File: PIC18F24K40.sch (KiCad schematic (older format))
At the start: 5 parts

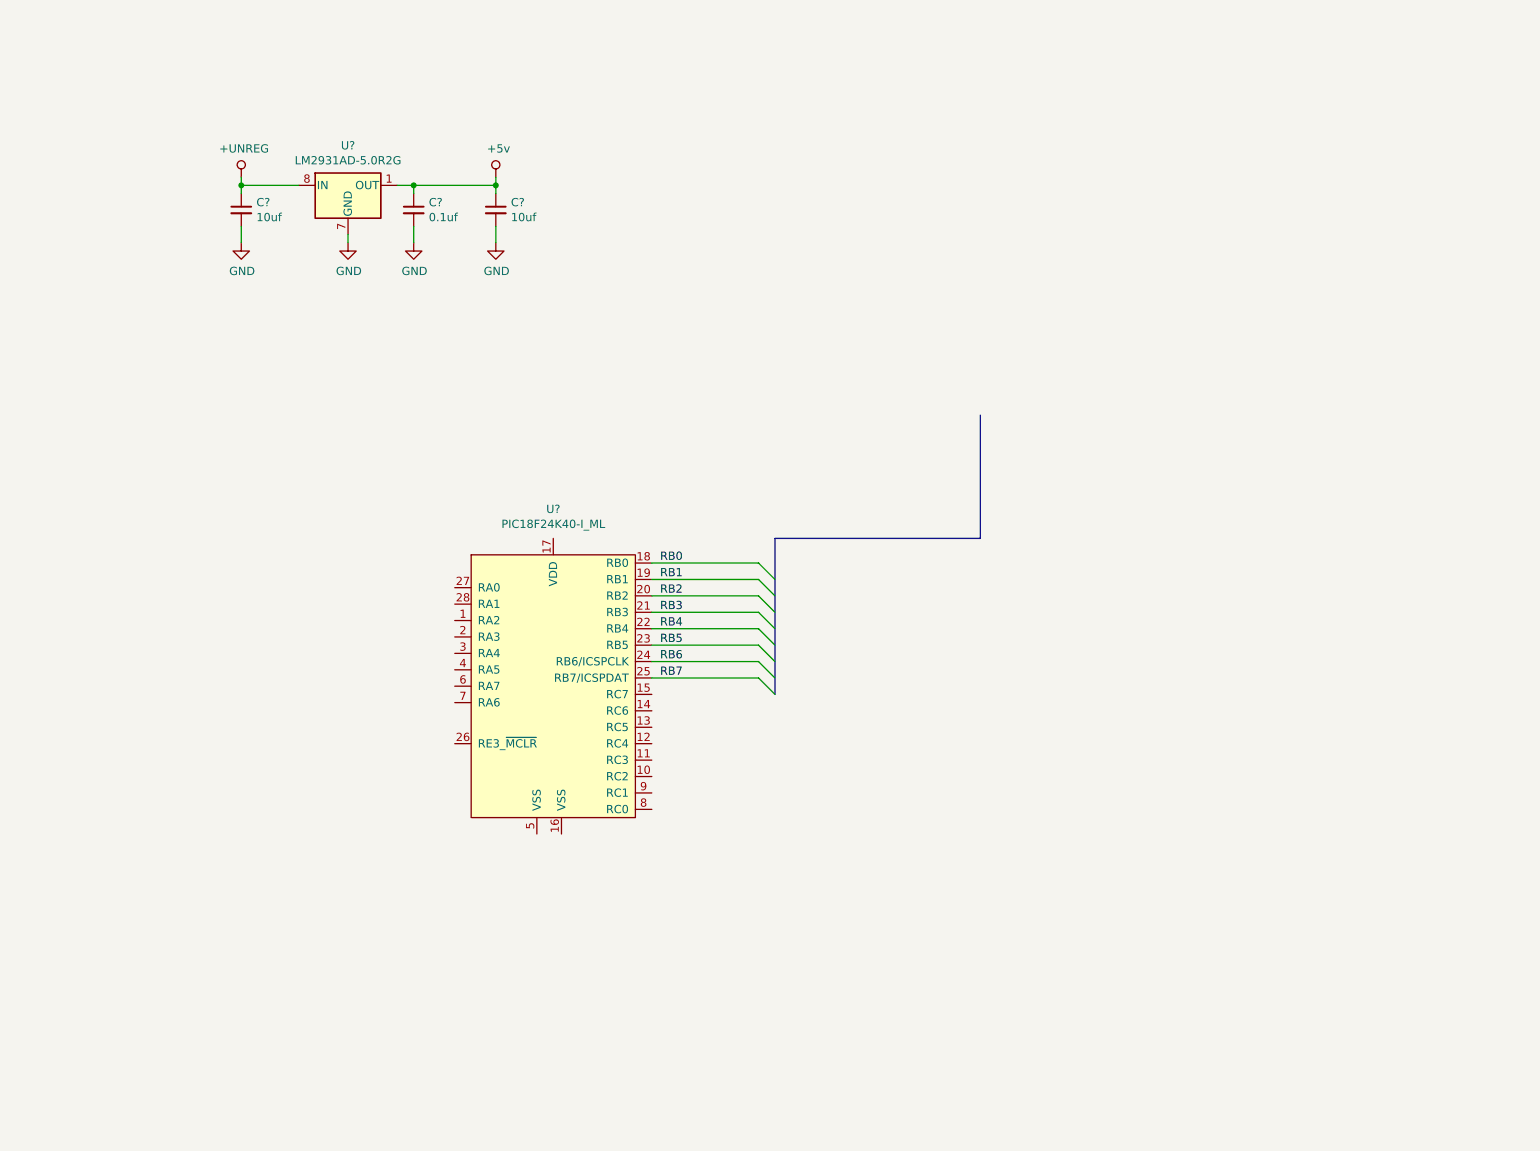
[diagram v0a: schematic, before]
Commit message: test board layout
I think I may want to drop the regulator
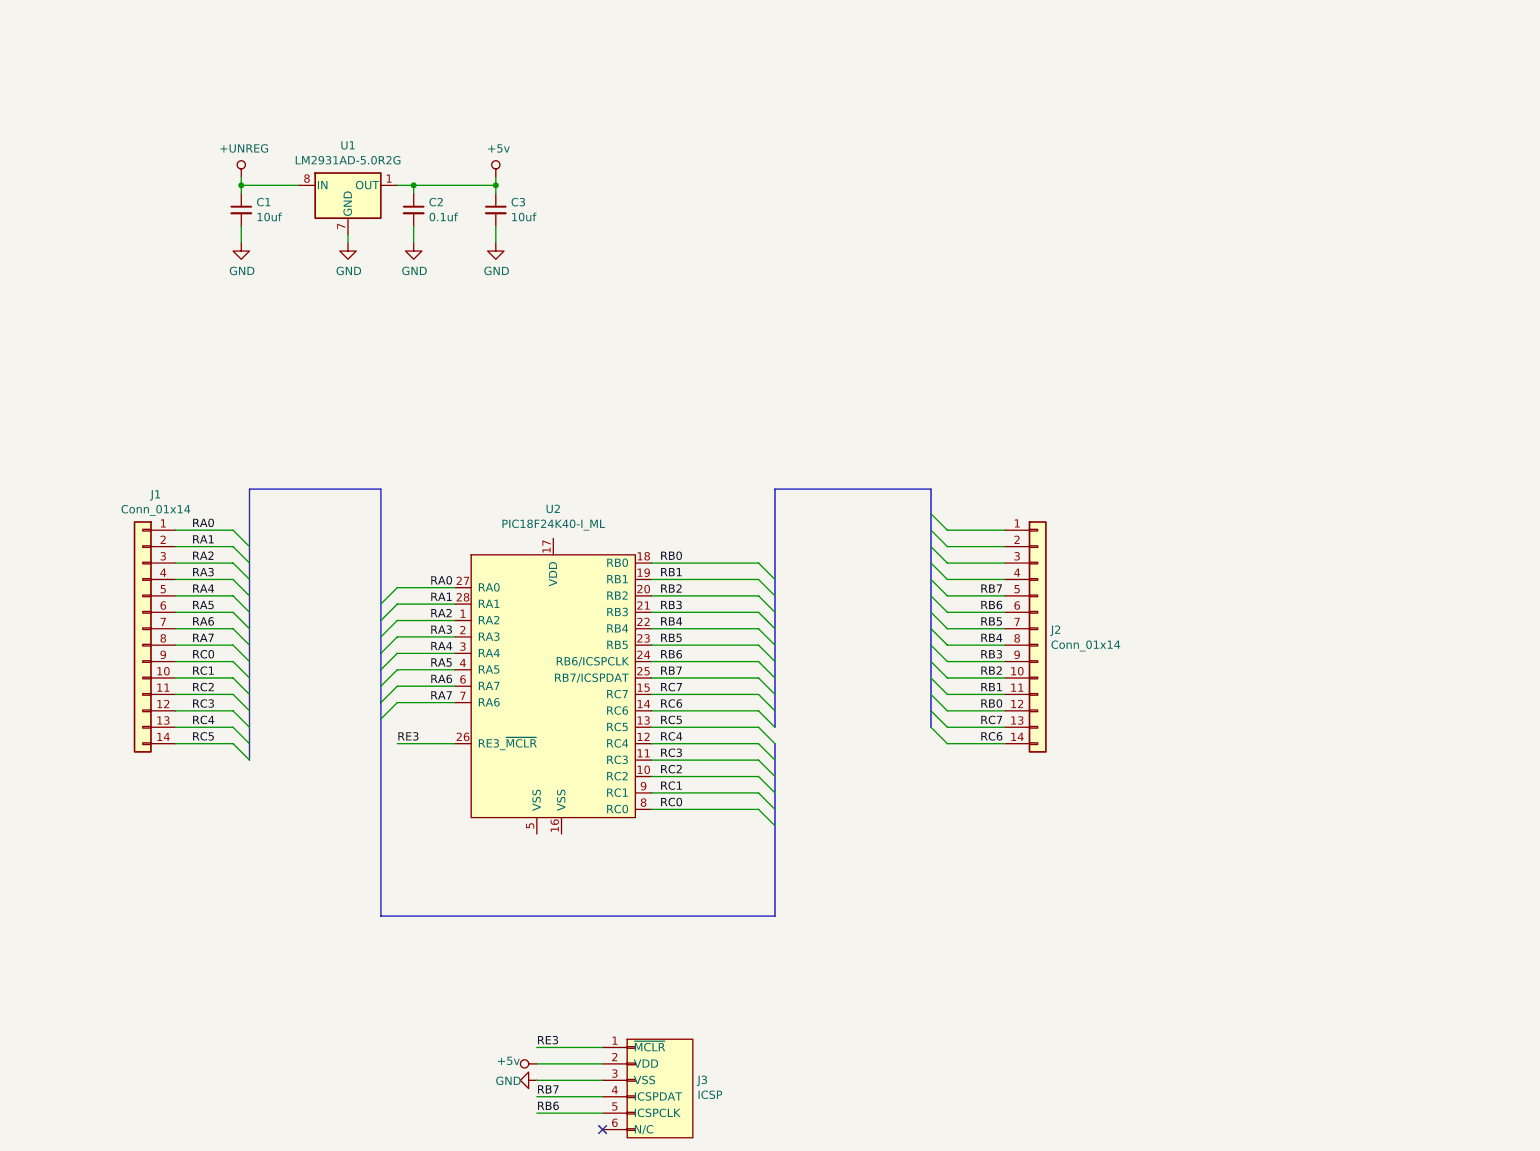
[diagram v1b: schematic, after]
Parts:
- added J1, J2: Conn_01x14, _PIC18F24K40:PinHeader_1x14_P2.54mm_Vertical, symbol _PIC18F24K40:Conn_01x14
- added J3: ICSP, _PIC18F24K40:PinHeader_1x06_P2.54mm_Vertical, symbol _PIC18F24K40:ICSP
- C1, C2, C3: renamed from C?; footprint (none) -> _PIC18F24K40:C_0603_1608Metric_Pad1.05x0.95mm_HandSolder
- U1: renamed from U?; footprint Package_SO:SOIC-8_3.9x4.9mm_P1.27mm -> _PIC18F24K40:SOIC-8_3.9x4.9mm_P1.27mm
- U2: renamed from U?; footprint (none) -> _PIC18F24K40:QFN-28-1EP_6x6mm_P0.65mm_EP4.25x4.25mm
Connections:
- net GND: now also J3.3 (VSS)
- net RB0: now also J2.12 (Pin_12)
- net RB1: now also J2.11 (Pin_11)
- net RB2: now also J2.10 (Pin_10)
- net RB3: now also J2.9 (Pin_9)
- net RB4: now also J2.8 (Pin_8)
- net RB5: now also J2.7 (Pin_7)
- net RB6: now also J2.6 (Pin_6), J3.5 (ICSPCLK)
- net RB7: now also J2.5 (Pin_5), J3.4 (ICSPDAT)
- net VCC: now also J3.2 (VDD)
- net RA2: now reaches U2.1 (RA2)
- net RA2: now also J1.3 (Pin_3)
- net RC2: now reaches U2.10 (RC2)
- net RC2: now also J1.11 (Pin_11)
- net RC3: now reaches U2.11 (RC3)
- net RC3: now also J1.12 (Pin_12)
- net RC4: now reaches U2.12 (RC4)
- net RC4: now also J1.13 (Pin_13)
- net RC5: now reaches U2.13 (RC5)
- net RC5: now also J1.14 (Pin_14)
- net RC6: now reaches U2.14 (RC6)
- net RC6: now also J2.14 (Pin_14)
- net RC7: now reaches U2.15 (RC7)
- net RC7: now also J2.13 (Pin_13)
- net RA3: now reaches U2.2 (RA3)
- net RA3: now also J1.4 (Pin_4)
- net RE3: now reaches U2.26 (RE3_~MCLR)
- net RE3: now also J3.1 (~MCLR)
- net RA0: now reaches U2.27 (RA0)
- net RA0: now also J1.1 (Pin_1)
- net RA1: now reaches U2.28 (RA1)
- net RA1: now also J1.2 (Pin_2)
- net RA4: now reaches U2.3 (RA4)
- net RA4: now also J1.5 (Pin_5)
- net RA5: now reaches U2.4 (RA5)
- net RA5: now also J1.6 (Pin_6)
- net RA6: now reaches U2.6 (RA7)
- net RA6: now also J1.7 (Pin_7)
- net RA7: now reaches U2.7 (RA6)
- net RA7: now also J1.8 (Pin_8)
- net RC0: now reaches U2.8 (RC0)
- net RC0: now also J1.9 (Pin_9)
- net RC1: now reaches U2.9 (RC1)
- net RC1: now also J1.10 (Pin_10)
- no-connect marks 0 -> 1

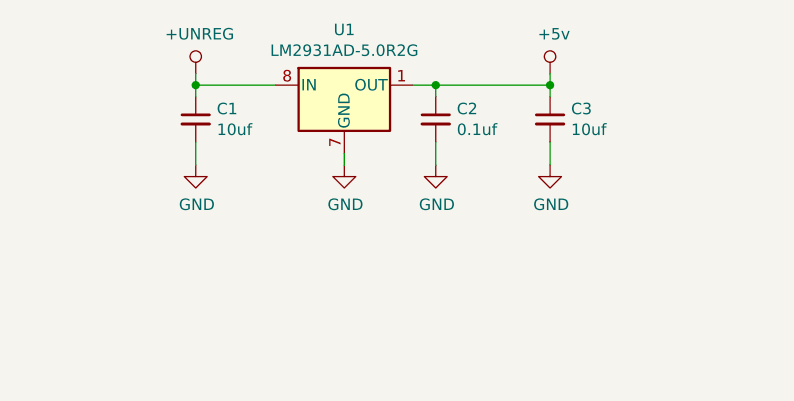
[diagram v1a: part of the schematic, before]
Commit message: Regulator removed
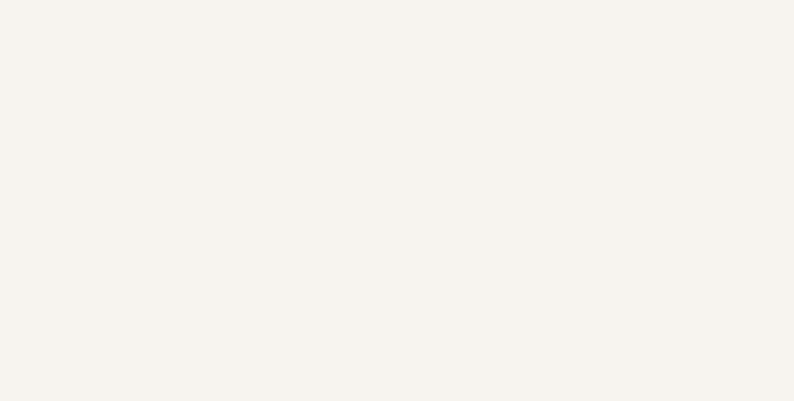
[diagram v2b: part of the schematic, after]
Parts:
- removed C1, C3: 10uf, _PIC18F24K40:C_0603_1608Metric_Pad1.05x0.95mm_HandSolder, symbol _PIC18F24K40:C_Small
- removed C2: 0.1uf, _PIC18F24K40:C_0603_1608Metric_Pad1.05x0.95mm_HandSolder, symbol _PIC18F24K40:C_Small
- removed U1: LM2931AD-5.0R2G, _PIC18F24K40:SOIC-8_3.9x4.9mm_P1.27mm, symbol _PIC18F24K40:LM2931AD-5.0R2G
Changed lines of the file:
@@
 $EndBitmap
-$Comp
-L _PIC18F24K40:LM2931AD-5.0R2G U1
-U 1 1 5BCEECB0
-P 2700 1600
-F 0 "U1" H 2700 1842 50  0000 C CNN
-F 1 "LM2931AD-5.0R2G" H 2700 1751 50  0000 C CNN
-F 2 "_PIC18F24K40:SOIC-8_3.9x4.9mm_P1.27mm" H 2800 1800 50  0001 C CIN
-F 3 "https://www.onsemi.com/pub/Collateral/LM2931-D.PDF" H 2900 1600 50  0001 C CNN
-	1    2700 1600
-	1    0    0    -1
-$EndComp
-$Comp
-L _PIC18F24K40:+UNREG #PWR0101
-U 1 1 5BCEF4FE
-P 2050 1550
-F 0 "#PWR0101" H 2050 1400 50  0001 C CNN
-F 1 "+UNREG" H 2067 1723 50  0000 C CNN
-F 2 "" H 2050 1550 50  0001 C CNN
-F 3 "" H 2050 1550 50  0001 C CNN
-	1    2050 1550
-	1    0    0    -1
-$EndComp
-$Comp
-L _PIC18F24K40:+5v #PWR0102
-U 1 1 5BCEF52A
-P 3600 1550
-F 0 "#PWR0102" H 3600 1400 50  0001 C CNN
-F 1 "+5v" H 3617 1723 50  0000 C CNN
-F 2 "" H 3600 1550 50  0001 C CNN
-F 3 "" H 3600 1550 50  0001 C CNN
-	1    3600 1550
-	1    0    0    -1
-$EndComp
-$Comp
-L _PIC18F24K40:C_Small C1
-U 1 1 5BCEF556
-P 2050 1750
-F 0 "C1" H 2142 1796 50  0000 L CNN
-F 1 "10uf" H 2142 1705 50  0000 L CNN
-F 2 "_PIC18F24K40:C_0603_1608Metric_Pad1.05x0.95mm_HandSolder" H 2050 1750 50  0001 C CNN
-F 3 "~" H 2050 1750 50  0001 C CNN
-	1    2050 1750
-	1    0    0    -1
-$EndComp
-$Comp
-L _PIC18F24K40:C_Small C2
-U 1 1 5BCEF5B4
-P 3100 1750
-F 0 "C2" H 3192 1796 50  0000 L CNN
-F 1 "0.1uf" H 3192 1705 50  0000 L CNN
-F 2 "_PIC18F24K40:C_0603_1608Metric_Pad1.05x0.95mm_HandSolder" H 3100 1750 50  0001 C CNN
-F 3 "~" H 3100 1750 50  0001 C CNN
-	1    3100 1750
-	1    0    0    -1
-$EndComp
-$Comp
-L _PIC18F24K40:C_Small C3
-U 1 1 5BCEF5FF
-P 3600 1750
-F 0 "C3" H 3692 1796 50  0000 L CNN
-F 1 "10uf" H 3692 1705 50  0000 L CNN
-F 2 "_PIC18F24K40:C_0603_1608Metric_Pad1.05x0.95mm_HandSolder" H 3600 1750 50  0001 C CNN
-F 3 "~" H 3600 1750 50  0001 C CNN
-	1    3600 1750
-	1    0    0    -1
-$EndComp
-Wire Wire Line
-	2400 1600 2050 1600
-Wire Wire Line
-	2050 1600 2050 1550
-Wire Wire Line
-	2050 1650 2050 1600
-Connection ~ 2050 1600
-Wire Wire Line
-	3600 1600 3600 1550
-Connection ~ 3600 1600
-Wire Wire Line
-	3600 1650 3600 1600
-Wire Wire Line
-	3000 1600 3100 1600
-Wire Wire Line
-	3100 1650 3100 1600
-Connection ~ 3100 1600
-Wire Wire Line
-	3100 1600 3600 1600
-$Comp
-L _PIC18F24K40:GND #PWR0103
-U 1 1 5BCEF72A
-P 2050 1950
-F 0 "#PWR0103" H 2050 1700 50  0001 C CNN
-F 1 "GND" H 2055 1777 50  0000 C CNN
-F 2 "" H 2050 1950 50  0001 C CNN
-F 3 "" H 2050 1950 50  0001 C CNN
-	1    2050 1950
-	1    0    0    -1
-$EndComp
-$Comp
-L _PIC18F24K40:GND #PWR0104
-U 1 1 5BCEF744
-P 2700 1950
-F 0 "#PWR0104" H 2700 1700 50  0001 C CNN
-F 1 "GND" H 2705 1777 50  0000 C CNN
-F 2 "" H 2700 1950 50  0001 C CNN
-F 3 "" H 2700 1950 50  0001 C CNN
-	1    2700 1950
-	1    0    0    -1
-$EndComp
-$Comp
-L _PIC18F24K40:GND #PWR0105
-U 1 1 5BCEF757
-P 3100 1950
-F 0 "#PWR0105" H 3100 1700 50  0001 C CNN
-F 1 "GND" H 3105 1777 50  0000 C CNN
-F 2 "" H 3100 1950 50  0001 C CNN
-F 3 "" H 3100 1950 50  0001 C CNN
-	1    3100 1950
-	1    0    0    -1
-$EndComp
-$Comp
-L _PIC18F24K40:GND #PWR0106
-U 1 1 5BCEF76A
-P 3600 1950
-F 0 "#PWR0106" H 3600 1700 50  0001 C CNN
-F 1 "GND" H 3605 1777 50  0000 C CNN
-F 2 "" H 3600 1950 50  0001 C CNN
-F 3 "" H 3600 1950 50  0001 C CNN
-	1    3600 1950
-	1    0    0    -1
-$EndComp
-Wire Wire Line
-	2050 1950 2050 1850
-Wire Wire Line
-	2700 1950 2700 1900
-Wire Wire Line
-	3100 1950 3100 1850
-Wire Wire Line
-	3600 1950 3600 1850
 $Comp
 L _PIC18F24K40:PIC18F24K40-I_ML U2

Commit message: Mostly cleanup
Backup and cache files are no longer versioned.

I've changed the breakout headers to 13 pin from 14 as we don't need
multiple power and ground pins broken out.

I think this board will be much more useful if it has the ability to
talk to a computer, so I'll be adding a part for the FTDI chip in the
reference folder, along with a USB type ? connector.

Currently the board is spaced to fit in a breadboard rather than
compatible with the arduino standard.
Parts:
- removed J1, J2: Conn_01x14, _PIC18F24K40:PinHeader_1x14_P2.54mm_Vertical, symbol _PIC18F24K40:Conn_01x14
- added J? (x2): Conn_01x13, _PIC18F24K40:PinHeader_1x13_P2.54mm_Vertical, symbol _PIC18F24K40:Conn_01x13
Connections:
- wire segments 58 -> 61
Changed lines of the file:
@@
 U 1 1 5BCEFCE3
 P 3900 4550
-F 0 "U2" H 3950 5528 50  0000 C CNN
-F 1 "PIC18F24K40-I_ML" H 3950 5437 50  0000 C CNN
+F 0 "U2" H 3550 5300 50  0000 C CNN
+F 1 "PIC18F24K40-I_ML" H 4350 5300 50  0000 C CNN
 F 2 "_PIC18F24K40:QFN-28-1EP_6x6mm_P0.65mm_EP4.25x4.25mm" H 3900 4550 50  0001 C CNN
 F 3 "" H 3900 4550 50  0001 C CNN
@@
 Text Label 4600 4600 0    50   ~ 0
 RB7
-$Comp
-L _PIC18F24K40:Conn_01x14 J2
-U 1 1 5BCFA54A
-P 6900 4300
-F 0 "J2" H 6980 4292 50  0000 L CNN
-F 1 "Conn_01x14" H 6980 4201 50  0000 L CNN
-F 2 "_PIC18F24K40:PinHeader_1x14_P2.54mm_Vertical" H 6900 4300 50  0001 C CNN
-F 3 "~" H 6900 4300 50  0001 C CNN
-	1    6900 4300
-	1    0    0    -1
-$EndComp
-$Comp
-L _PIC18F24K40:Conn_01x14 J1
-U 1 1 5BCFA73A
-P 1450 4300
-F 0 "J1" H 1370 5117 50  0000 C CNN
-F 1 "Conn_01x14" H 1370 5026 50  0000 C CNN
-F 2 "_PIC18F24K40:PinHeader_1x14_P2.54mm_Vertical" H 1450 4300 50  0001 C CNN
-F 3 "~" H 1450 4300 50  0001 C CNN
-	1    1450 4300
-	-1   0    0    -1
-$EndComp
 Entry Wire Line
 	5200 4700 5300 4800
@@
 Entry Wire Line
 	2000 4900 2100 5000
-Entry Wire Line
-	2000 5000 2100 5100
 Wire Wire Line
 	2000 3700 1650 3700
@@
 Wire Wire Line
 	2000 4900 1650 4900
-Wire Wire Line
-	2000 5000 1650 5000
-Entry Wire Line
-	6250 3700 6350 3800
-Entry Wire Line
-	6250 3600 6350 3700
 Entry Wire Line
 	6250 3900 6350 4000
 Entry Wire Line
-	6250 3800 6350 3900
-Entry Wire Line
 	6250 4000 6350 4100
 Entry Wire Line
@@
 Entry Wire Line
 	6250 4900 6350 5000
-Wire Wire Line
-	6700 3700 6350 3700
-Wire Wire Line
-	6700 3800 6350 3800
-Wire Wire Line
-	6350 3900 6700 3900
 Wire Wire Line
 	6700 4000 6350 4000
@@
 Text Label 1750 4900 0    50   ~ 0
 RC4
-Text Label 1750 5000 0    50   ~ 0
+Text Label 6550 5000 0    50   ~ 0
 RC5
-Text Label 6550 5000 0    50   ~ 0
+Text Label 6550 4900 0    50   ~ 0
 RC6
-Text Label 6550 4900 0    50   ~ 0
+Text Label 6550 4800 0    50   ~ 0
 RC7
-Text Label 6550 4800 0    50   ~ 0
+Text Label 6550 4700 0    50   ~ 0
 RB0
-Text Label 6550 4700 0    50   ~ 0
+Text Label 6550 4600 0    50   ~ 0
 RB1
-Text Label 6550 4600 0    50   ~ 0
+Text Label 6550 4500 0    50   ~ 0
 RB2
-Text Label 6550 4500 0    50   ~ 0
+Text Label 6550 4400 0    50   ~ 0
 RB3
-Text Label 6550 4400 0    50   ~ 0
+Text Label 6550 4300 0    50   ~ 0
 RB4
-Text Label 6550 4300 0    50   ~ 0
+Text Label 6550 4200 0    50   ~ 0
 RB5
-Text Label 6550 4200 0    50   ~ 0
+Text Label 6550 4100 0    50   ~ 0
 RB6
-Text Label 6550 4100 0    50   ~ 0
+Text Label 6550 4000 0    50   ~ 0
 RB7
 $Comp
@@
 Text Label 3850 6850 0    50   ~ 0
 RE3
-Wire Bus Line
-	5300 5000 5300 6050
+$Comp
+L _PIC18F24K40:Conn_01x13 J?
+U 1 1 5BD10226
+P 1450 4300
+F 0 "J?" H 1370 5117 50  0000 C CNN
+F 1 "Conn_01x13" H 1370 5026 50  0000 C CNN
+F 2 "_PIC18F24K40:PinHeader_1x13_P2.54mm_Vertical" H 1450 4300 50  0001 C CNN
+F 3 "~" H 1450 4300 50  0001 C CNN
+	1    1450 4300
+	-1   0    0    -1
+$EndComp
+$Comp
+L _PIC18F24K40:Conn_01x13 J?
+U 1 1 5BD14518
+P 6900 4400
+F 0 "J?" H 6980 4442 50  0000 L CNN
+F 1 "Conn_01x13" H 6980 4351 50  0000 L CNN
+F 2 "_PIC18F24K40:PinHeader_1x13_P2.54mm_Vertical" H 6900 4400 50  0001 C CNN
+F 3 "~" H 6900 4400 50  0001 C CNN
+	1    6900 4400
+	1    0    0    -1
+$EndComp
+$Comp
+L _PIC18F24K40:+5v #PWR?
+U 1 1 5BD1682D
+P 6550 3800
+F 0 "#PWR?" H 6550 3650 50  0001 C CNN
+F 1 "+5v" V 6567 3973 50  0000 C CNN
+F 2 "" H 6550 3800 50  0001 C CNN
+F 3 "" H 6550 3800 50  0001 C CNN
+	1    6550 3800
+	0    -1   -1   0
+$EndComp
+$Comp
+L _PIC18F24K40:GND #PWR?
+U 1 1 5BD1690C
+P 6550 3900
+F 0 "#PWR?" H 6550 3650 50  0001 C CNN
+F 1 "GND" V 6555 3727 50  0000 C CNN
+F 2 "" H 6550 3900 50  0001 C CNN
+F 3 "" H 6550 3900 50  0001 C CNN
+	1    6550 3900
+	0    1    1    0
+$EndComp
+Wire Wire Line
+	6700 3800 6550 3800
+Wire Wire Line
+	6700 3900 6550 3900
+$Comp
+L _PIC18F24K40:+5v #PWR?
+U 1 1 5BD1A8A9
+P 3950 3700
+F 0 "#PWR?" H 3950 3550 50  0001 C CNN
+F 1 "+5v" H 3967 3873 50  0000 C CNN
+F 2 "" H 3950 3700 50  0001 C CNN
+F 3 "" H 3950 3700 50  0001 C CNN
+	1    3950 3700
+	1    0    0    -1
+$EndComp
+$Comp
+L _PIC18F24K40:GND #PWR?
+U 1 1 5BD1A8CD
+P 3900 5650
+F 0 "#PWR?" H 3900 5400 50  0001 C CNN
+F 1 "GND" H 3905 5477 50  0000 C CNN
+F 2 "" H 3900 5650 50  0001 C CNN
+F 3 "" H 3900 5650 50  0001 C CNN
+	1    3900 5650
+	1    0    0    -1
+$EndComp
+Wire Wire Line
+	3850 5550 3850 5650
+Wire Wire Line
+	3850 5650 3900 5650
+Wire Wire Line
+	4000 5650 3900 5650
+Connection ~ 3900 5650
+Wire Wire Line
+	4000 5550 4000 5650
+Wire Wire Line
+	3950 3750 3950 3700
+Wire Bus Line
+	5300 5100 5300 6050
 Wire Bus Line
 	2900 3450 2900 6050
 Wire Bus Line
-	5300 3450 5300 4900
-Wire Bus Line
-	2100 3450 2100 5100
+	5300 3450 5300 5000
 Wire Bus Line
 	6250 3450 6250 4900
+Wire Bus Line
+	2100 3450 2100 5000
 $EndSCHEMATC
